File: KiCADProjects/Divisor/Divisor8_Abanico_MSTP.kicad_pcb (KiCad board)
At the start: 2 copper layers, 71.1 x 91 mm, 18 parts, among them J1 SMA_Female, J2 SMA_Female, J3 SMA_Female, J4 SMA_Female, J5 SMA_Female, J6 SMA_Female, J7 SMA_Female, J8 SMA_Female, J9 SMA_Female

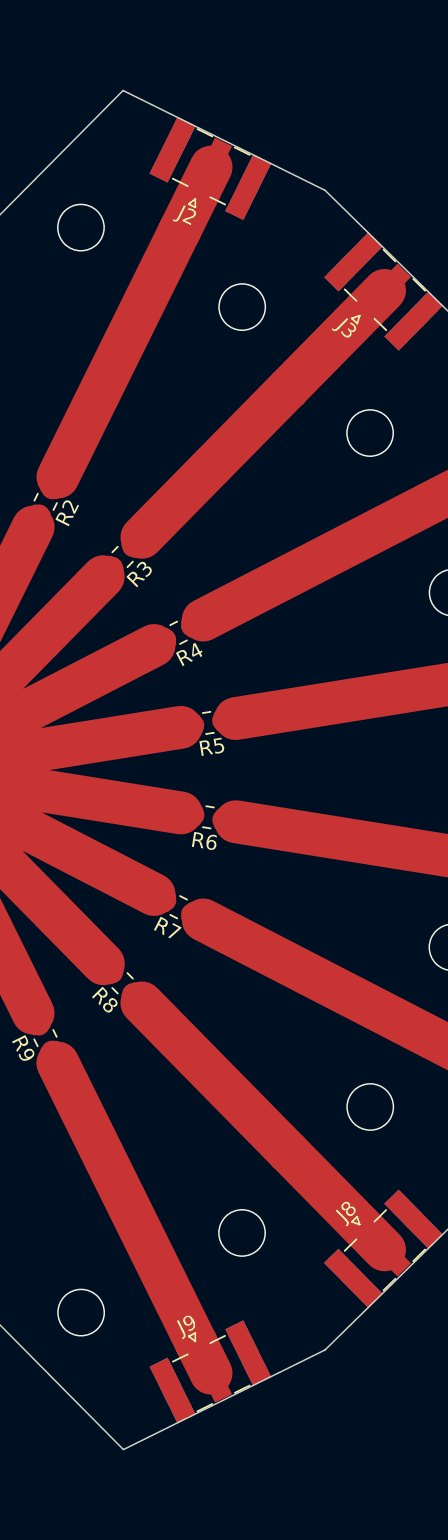
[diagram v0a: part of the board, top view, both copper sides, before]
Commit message: Versión con sys clk a 100 MHz. Archivos de proyecto
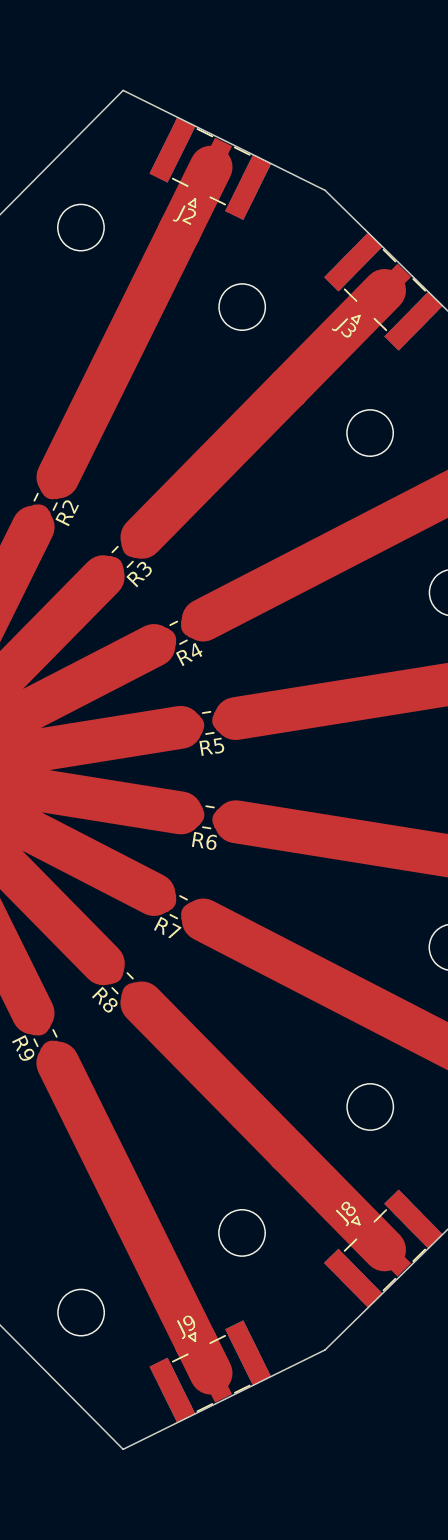
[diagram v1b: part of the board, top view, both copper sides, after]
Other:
- board size 71.1 x 91 mm -> 71.1 x 90.9 mm
